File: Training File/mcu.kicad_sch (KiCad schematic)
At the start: 2 parts, among them J2 8P8C_LED_Shielded, U1 Teensy4.1_DEV-16771

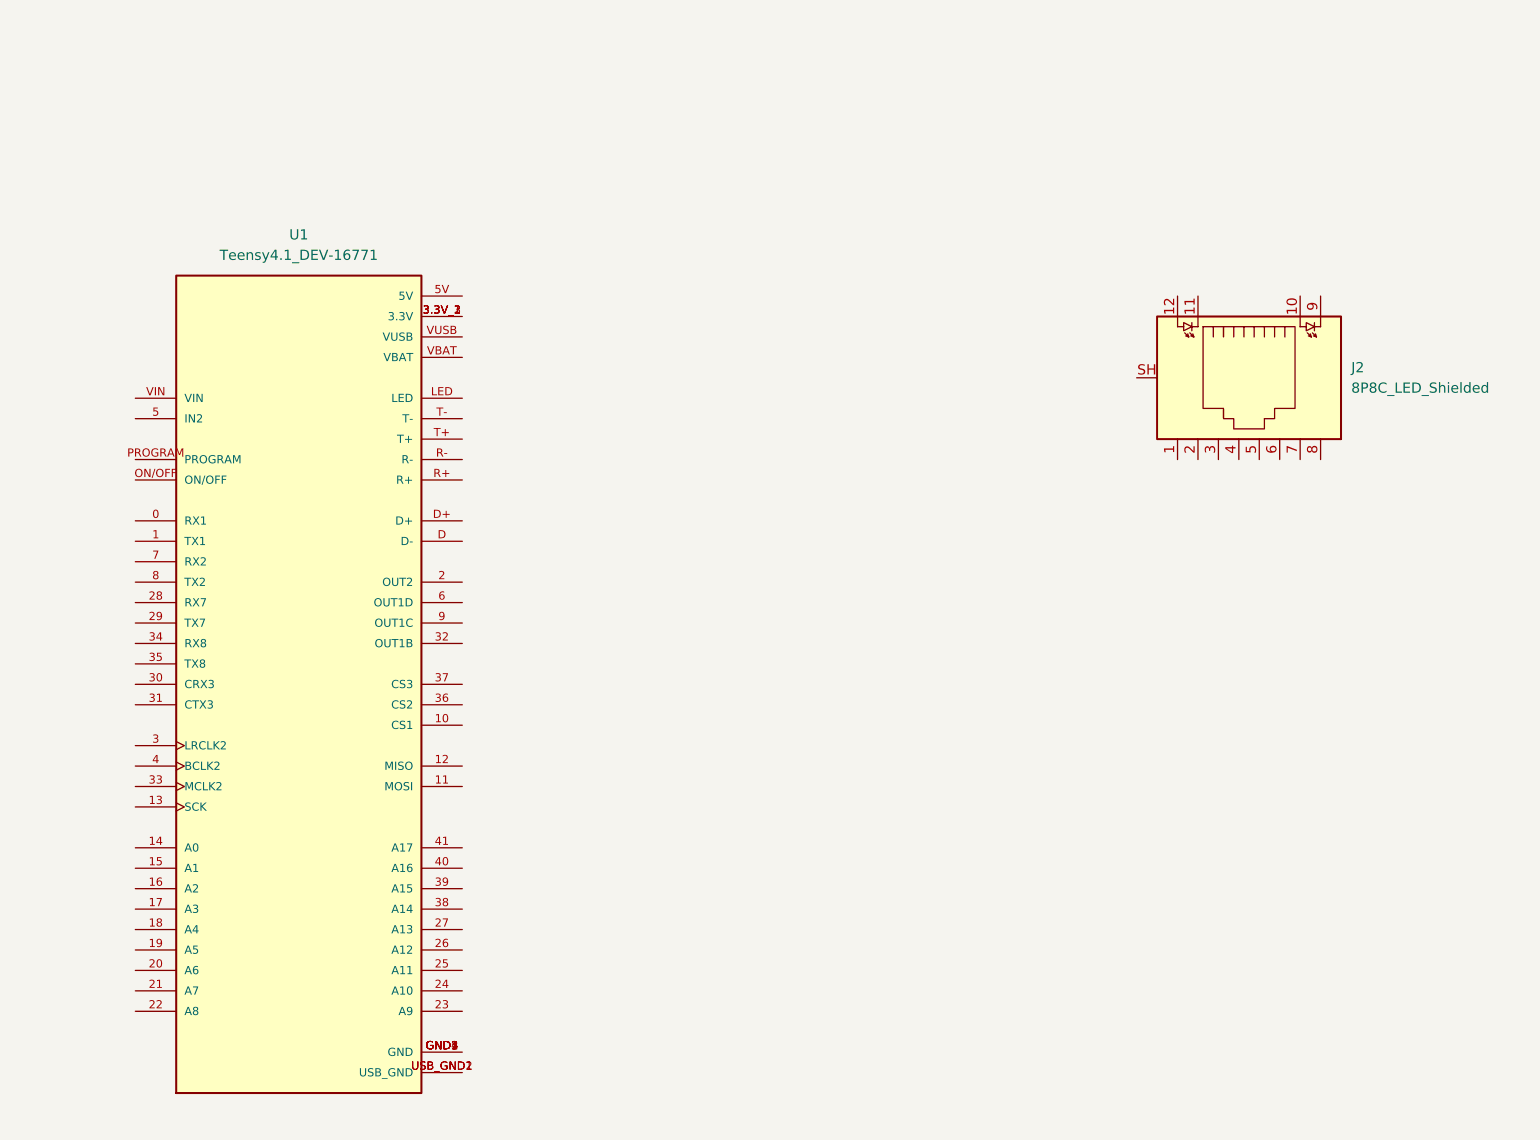
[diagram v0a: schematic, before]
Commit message: Add ethernet
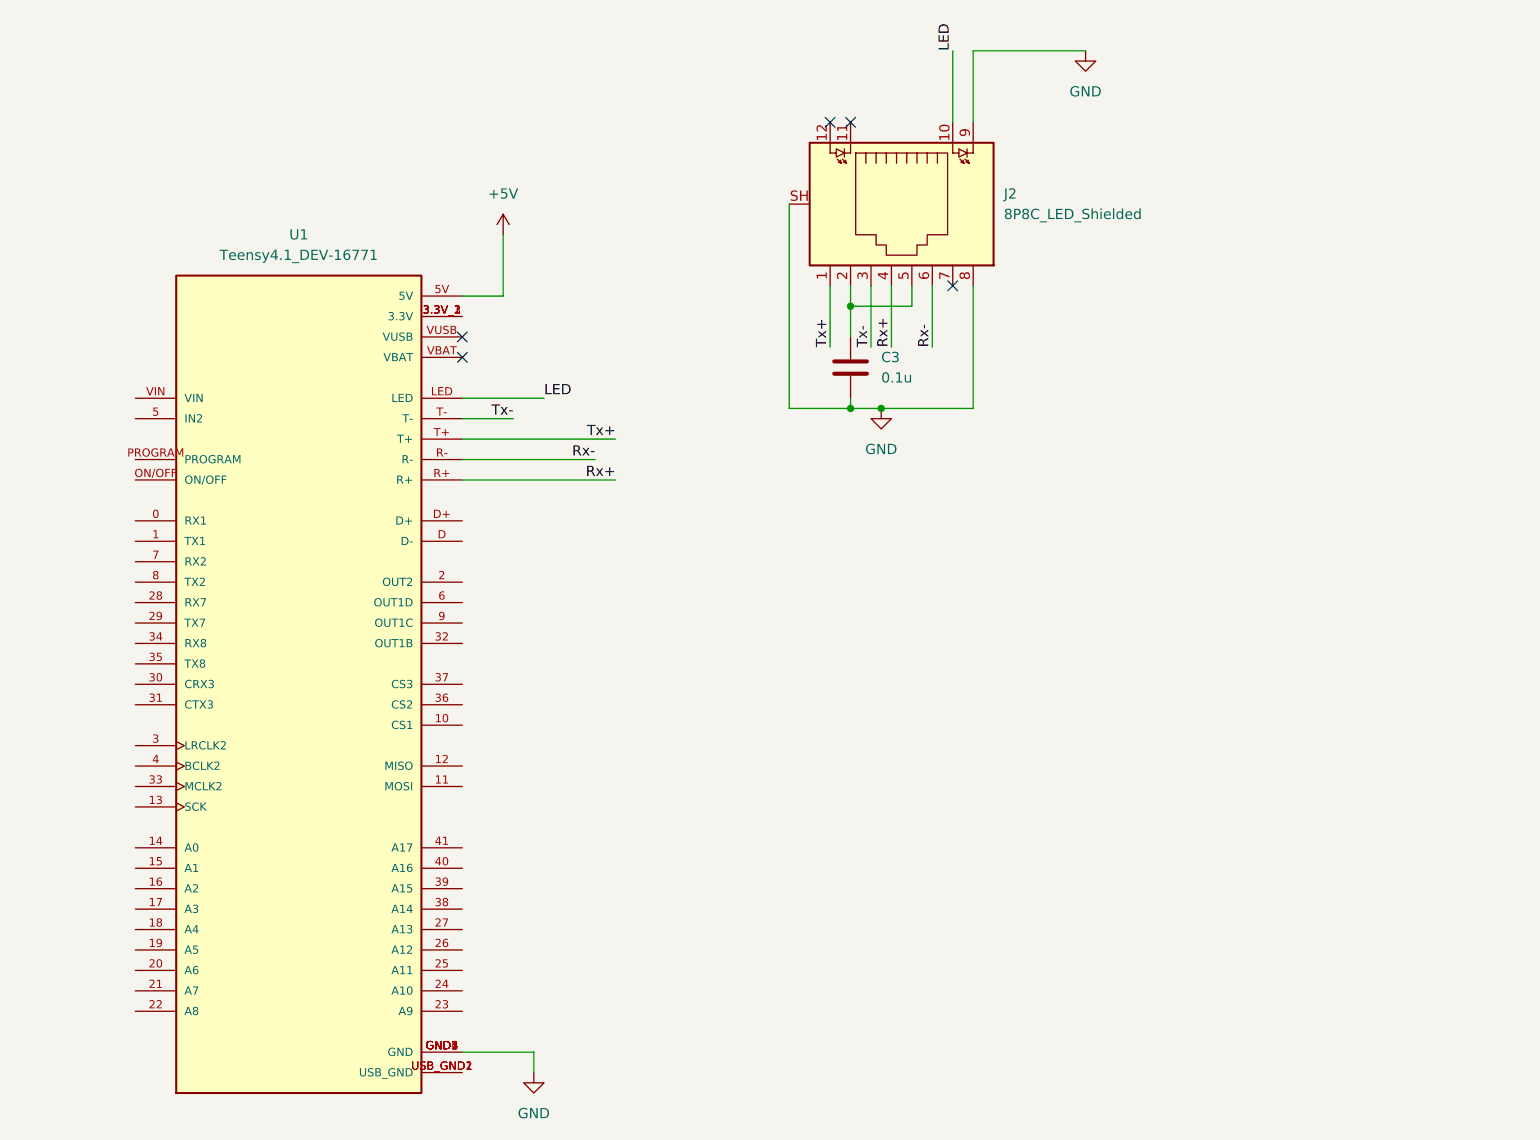
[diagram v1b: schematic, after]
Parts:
- added C3: 0.1u, symbol Device:C
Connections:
- net Tx+: now reaches J2.1
- net Tx+: now also U1.T+
- net LED: now reaches J2.10
- net LED: now also U1.LED
- net at J2.2: now also J2.5, C3.1
- net Tx-: now reaches J2.3
- net Tx-: now also U1.T-
- net Rx+: now reaches J2.4
- net Rx+: now also U1.R+
- net Rx-: now reaches J2.6
- net Rx-: now also U1.R-
- net GND: now reaches J2.8
- net GND: now also J2.9, J2.SH, U1.GND1 (GND), U1.GND2 (GND), U1.GND3 (GND), U1.GND4 (GND), U1.GND5 (GND), C3.2
- net +5V: now reaches U1.5V
- no-connect marks 0 -> 5
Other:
- moved on the sheet: J2

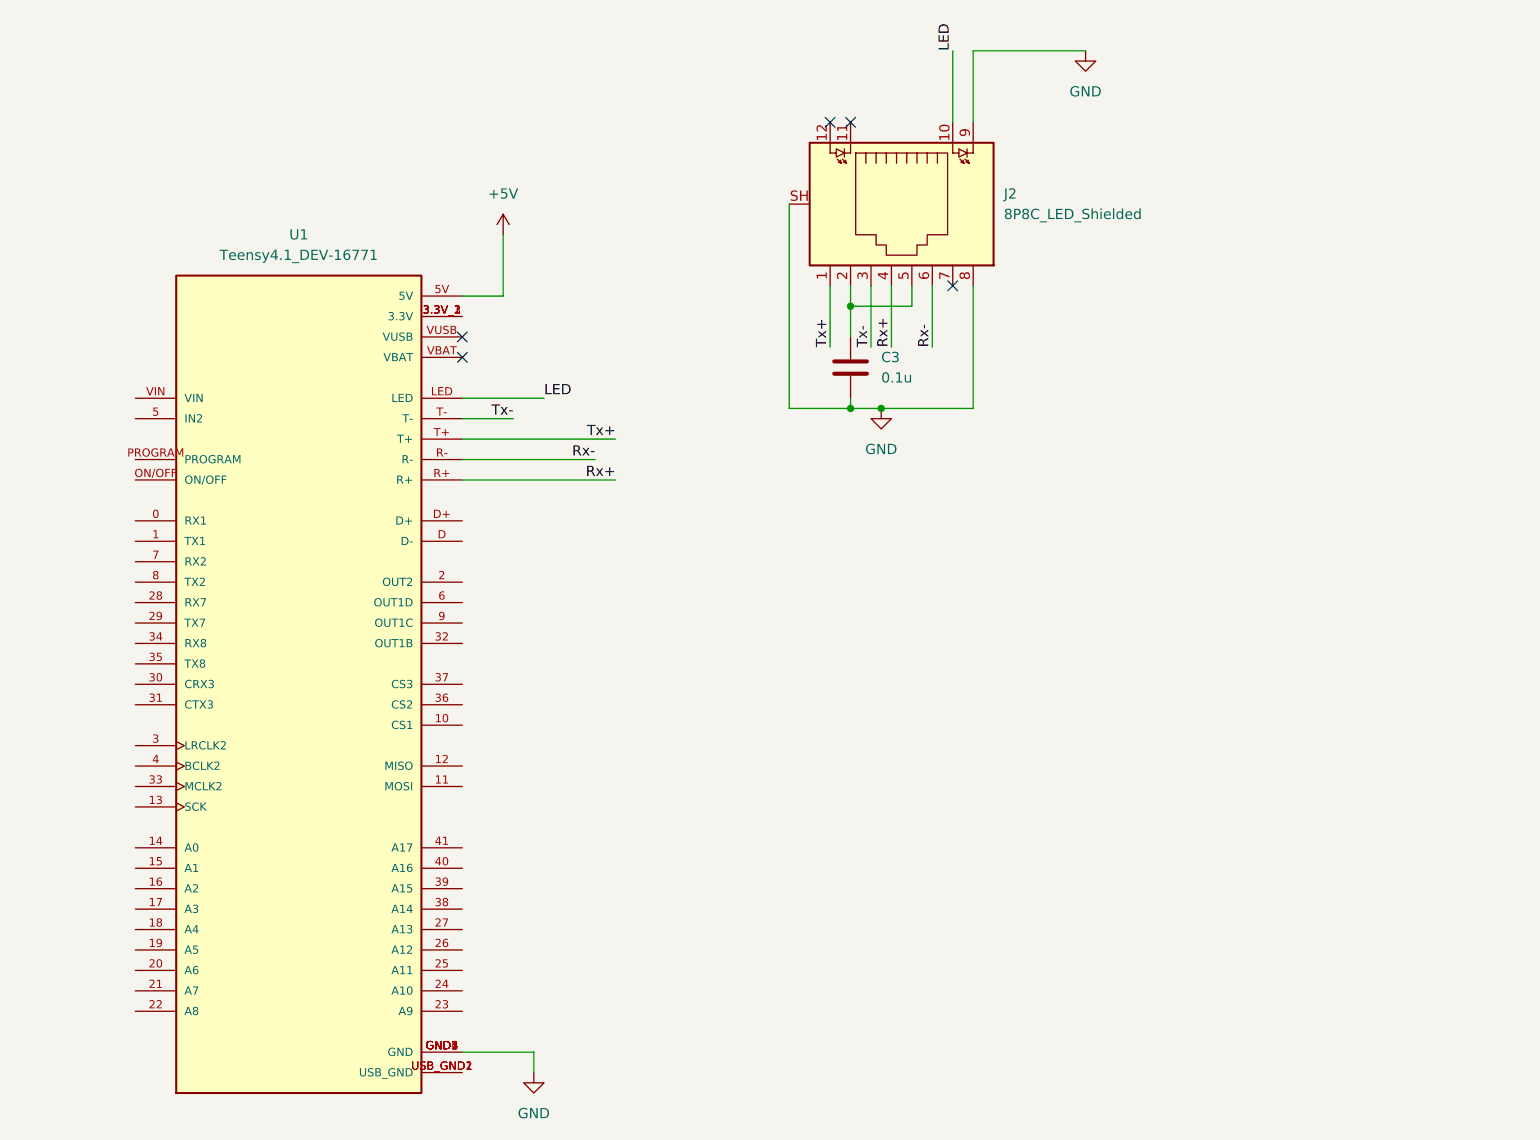
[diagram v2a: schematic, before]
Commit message: Finish schematic
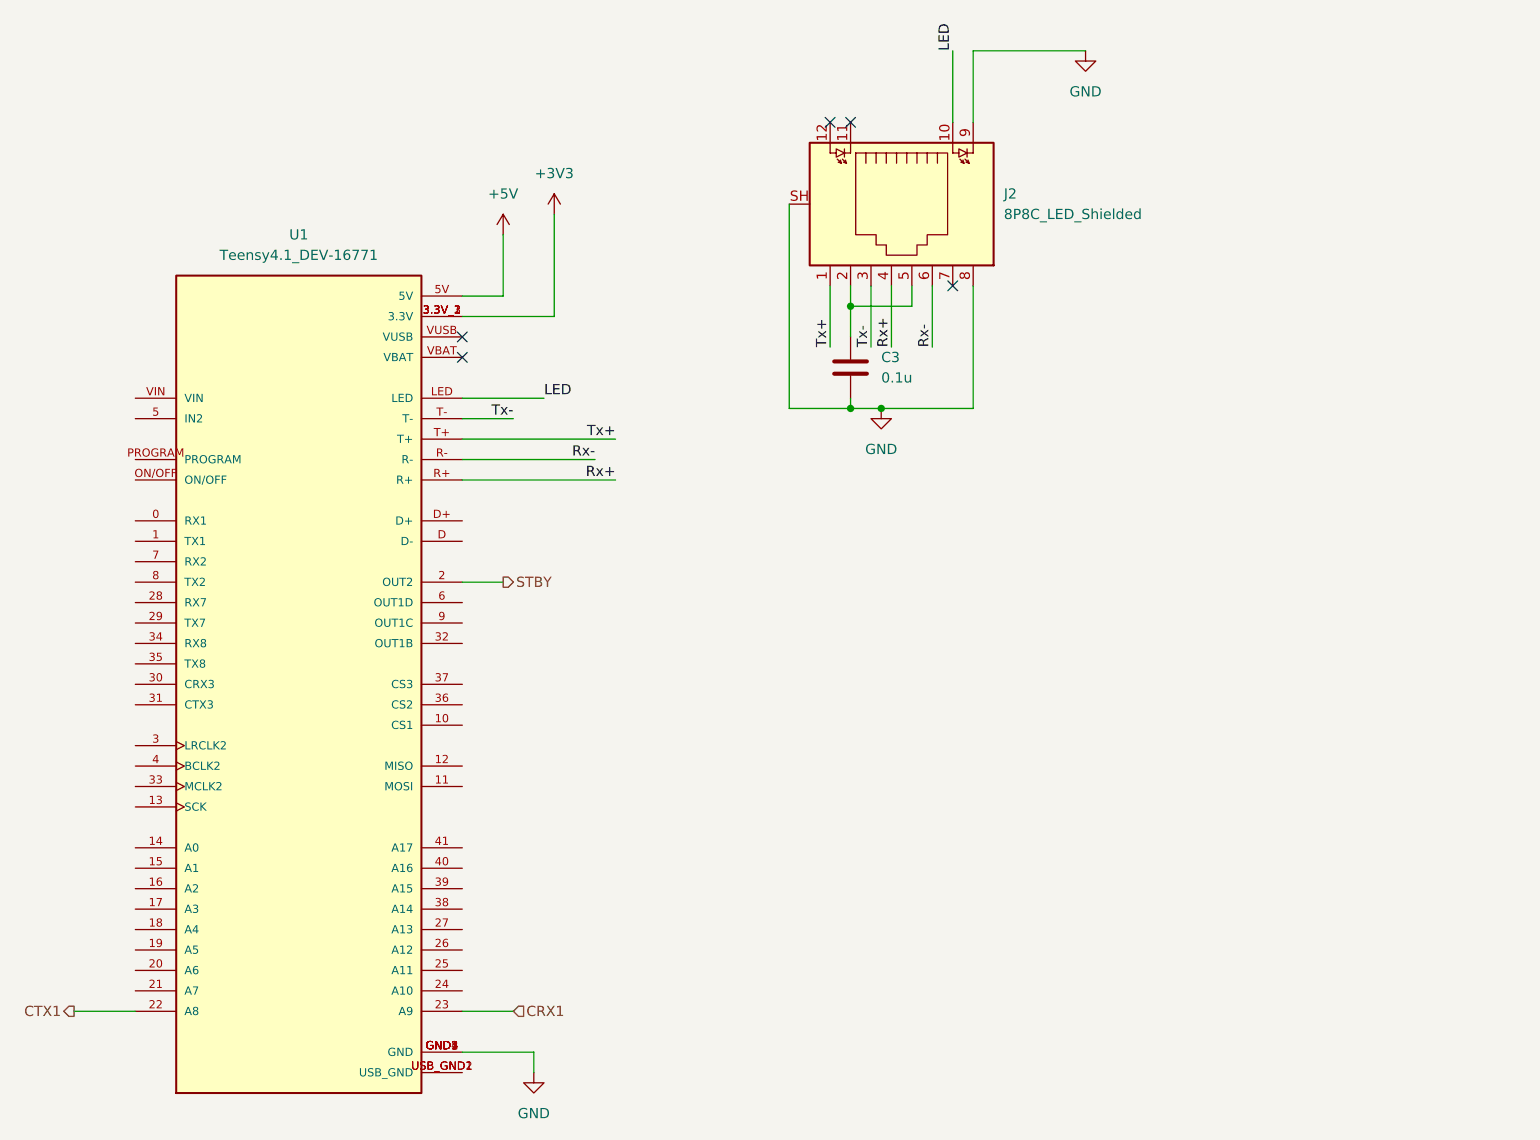
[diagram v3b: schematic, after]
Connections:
- net STBY: now reaches U1.2 (OUT2)
- net CTX1: now reaches U1.22 (A8)
- net CRX1: now reaches U1.23 (A9)
- net +3V3: now reaches U1.3.3V_1 (3.3V), U1.3.3V_2 (3.3V), U1.3.3V_3 (3.3V)
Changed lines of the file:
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@@
+	(wire
+		(pts
+			(xy 76.2 54.61) (xy 87.63 54.61)
+		)
+		(stroke
+			(width 0)
+			(type default)
+		)
+	)
+	(wire
+		(pts
+			(xy 76.2 140.97) (xy 82.55 140.97)
+		)
+		(stroke
+			(width 0)
+			(type default)
+		)
+	)
 	(wire
 		(pts
@@
 	(wire
 		(pts
+			(xy 76.2 87.63) (xy 81.28 87.63)
+		)
+		(stroke
+			(width 0)
+			(type default)
+		)
+	)
+	(wire
+		(pts
 			(xy 85.09 148.59) (xy 85.09 146.05)
 		)
@@
 	(wire
 		(pts
+			(xy 87.63 41.91) (xy 87.63 54.61)
+		)
+		(stroke
+			(width 0)
+			(type default)
+		)
+	)
+	(wire
+		(pts
 			(xy 85.09 146.05) (xy 76.2 146.05)
 		)
@@
 		(pts
 			(xy 121.92 50.8) (xy 121.92 58.42)
+		)
+		(stroke
+			(width 0)
+			(type default)
+		)
+	)
+	(wire
+		(pts
+			(xy 27.94 140.97) (xy 35.56 140.97)
 		)
 		(stroke
@@
 			)
 			(justify left bottom)
+		)
+	)
+	(hierarchical_label "STBY"
+		(shape output)
+		(at 81.28 87.63 0)
+		(effects
+			(font
+				(size 1.27 1.27)
+			)
+			(justify left)
+		)
+	)
+	(hierarchical_label "CRX1"
+		(shape input)
+		(at 82.55 140.97 0)
+		(effects
+			(font
+				(size 1.27 1.27)
+			)
+			(justify left)
+		)
+	)
+	(hierarchical_label "CTX1"
+		(shape output)
+		(at 27.94 140.97 180)
+		(effects
+			(font
+				(size 1.27 1.27)
+			)
+			(justify right)
 		)
 	)
@@
 					(unit 1)
 				)
+			)
+		)
+	)
+	(symbol
+		(lib_id "power:+3V3")
+		(at 87.63 41.91 0)
+		(unit 1)
+		(exclude_from_sim no)
+		(in_bom yes)
+		(on_board yes)
+		(dnp no)
+		(fields_autoplaced yes)
+		(property "Reference" "#PWR012"
+			(at 87.63 45.72 0)
+			(effects
+				(font
+					(size 1.27 1.27)
+				)
+				(hide yes)
+			)
+		)
+		(property "Value" "+3V3"
+			(at 87.63 36.83 0)
+			(effects
+				(font
+					(size 1.27 1.27)
+				)
+			)
+		)
+		(property "Footprint" ""
+			(at 87.63 41.91 0)
+			(effects
+				(font
+					(size 1.27 1.27)
+				)
+				(hide yes)
+			)
+		)
+		(property "Datasheet" ""
+			(at 87.63 41.91 0)
+			(effects
+				(font
+					(size 1.27 1.27)
+				)
+				(hide yes)
+			)
+		)
+		(property "Description" "Power symbol creates a global label with name \"+3V3\""
+			(at 87.63 41.91 0)
+			(effects
+				(font
+					(size 1.27 1.27)
+				)
+				(hide yes)
+			)
+		)
+		(pin "1"
+		)
+		(instances
+			(project ""
+				(path "/d3b46590-8d43-4cdb-9712-6960f55d7470/5d97ce7e-36bf-4bc0-9fcd-cf3ccf089b00"
+					(reference "#PWR012")
+					(unit 1)
+				)
